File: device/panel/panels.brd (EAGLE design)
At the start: 133 x 77 mm, 0 parts

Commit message: More panel work.
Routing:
- added copper zone on layer 16, net S$1
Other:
- board size 133 x 77 mm -> 132.9 x 80 mm

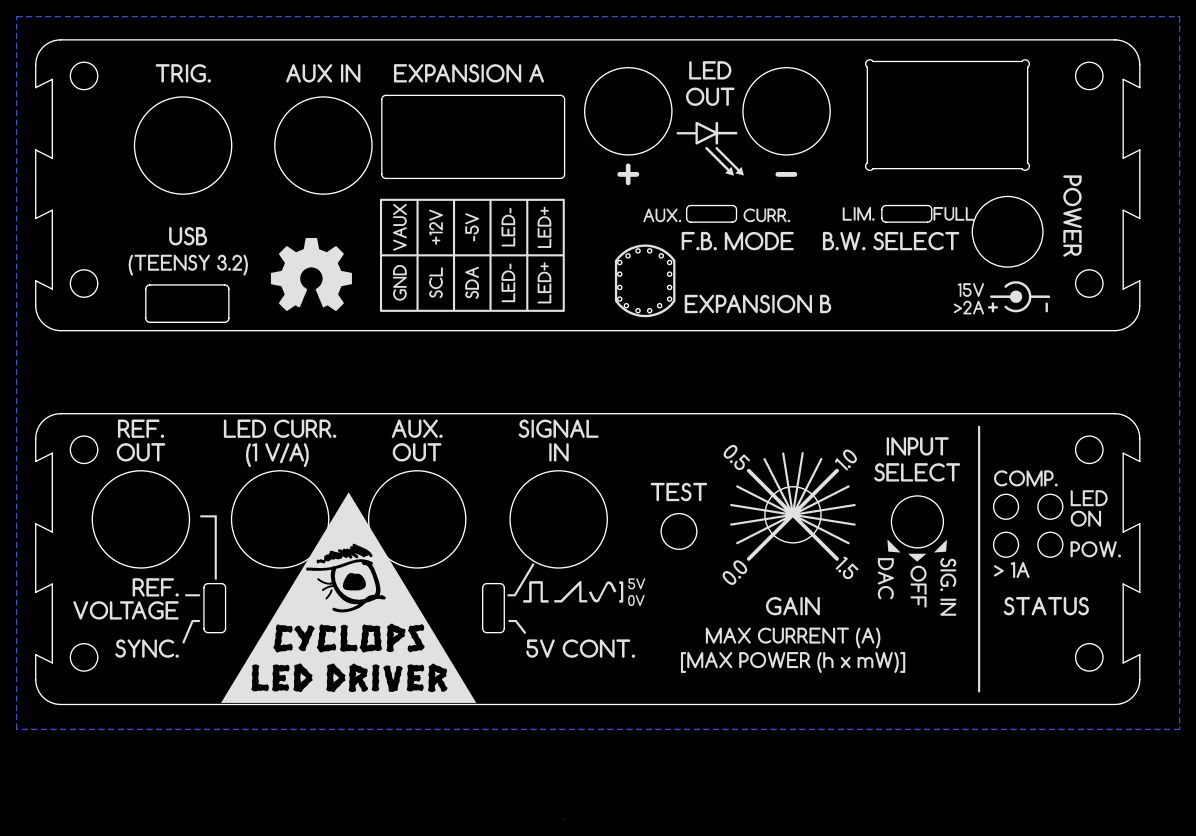
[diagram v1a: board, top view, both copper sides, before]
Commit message: Panels and final protoboard sent to production.
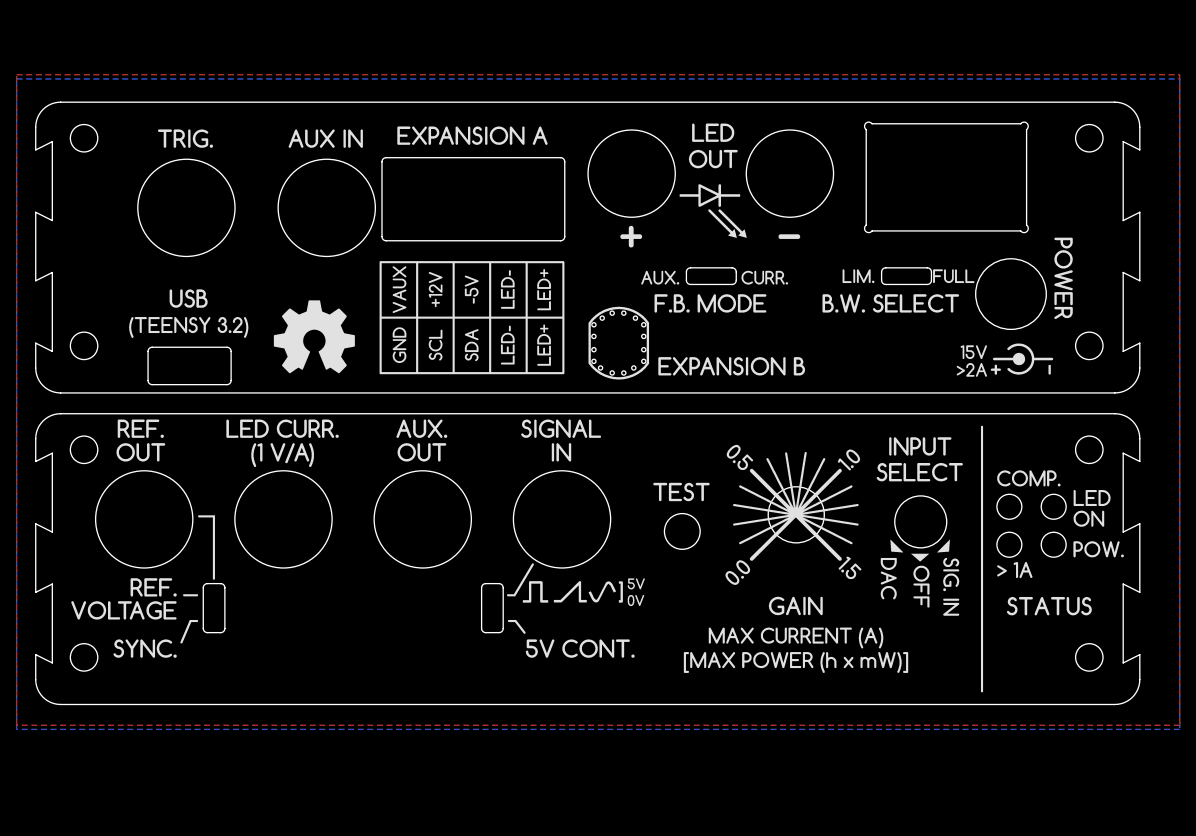
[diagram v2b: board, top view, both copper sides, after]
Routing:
- added copper zone on layer 1, net S$1
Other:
- board size 132.9 x 80 mm -> 132.9 x 72.5 mm

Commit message: Panel fixes after testing.
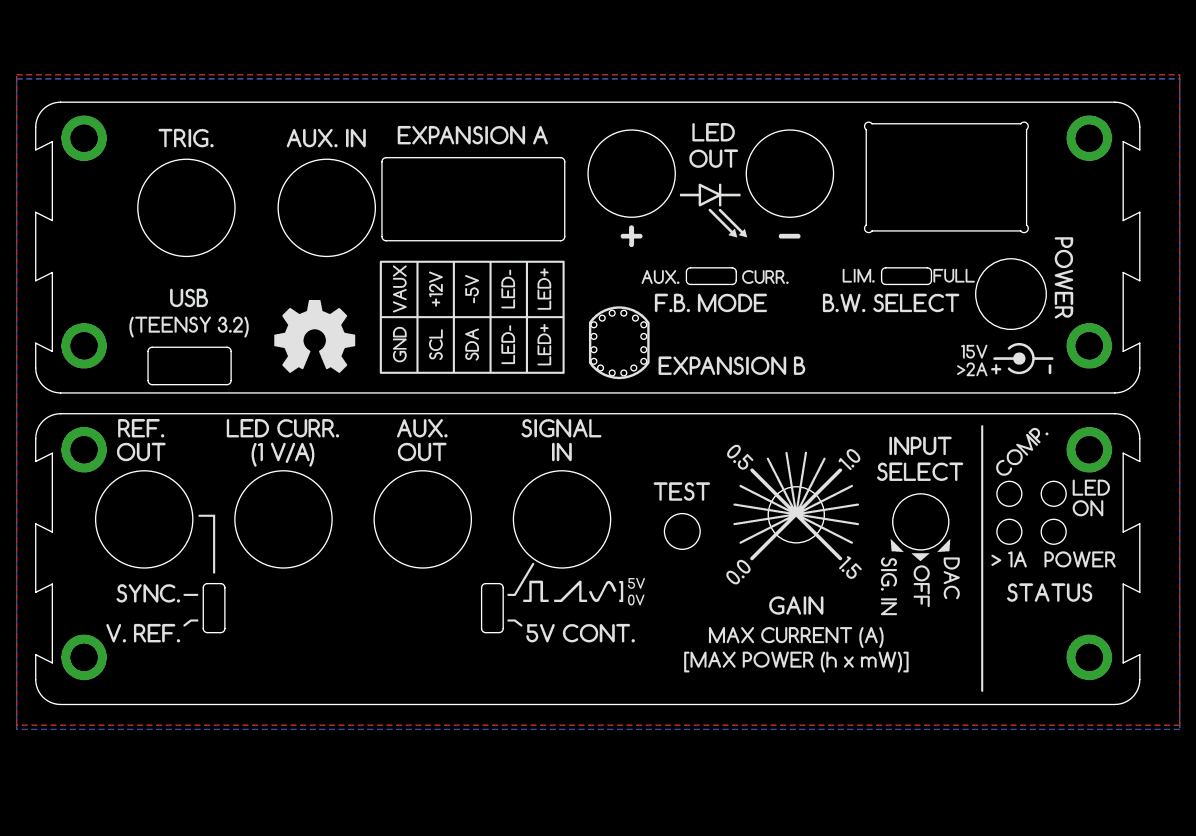
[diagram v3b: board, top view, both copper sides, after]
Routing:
- added copper zone on layer 1, net GND
- added copper zone on layer 16, net GND
- removed copper zone on layer 1, net S$1
- removed copper zone on layer 16, net S$1

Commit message: Ready for 3.6 production
- These designs are up to date for 3.6 production
- I need to create an assembly manual before moving forward
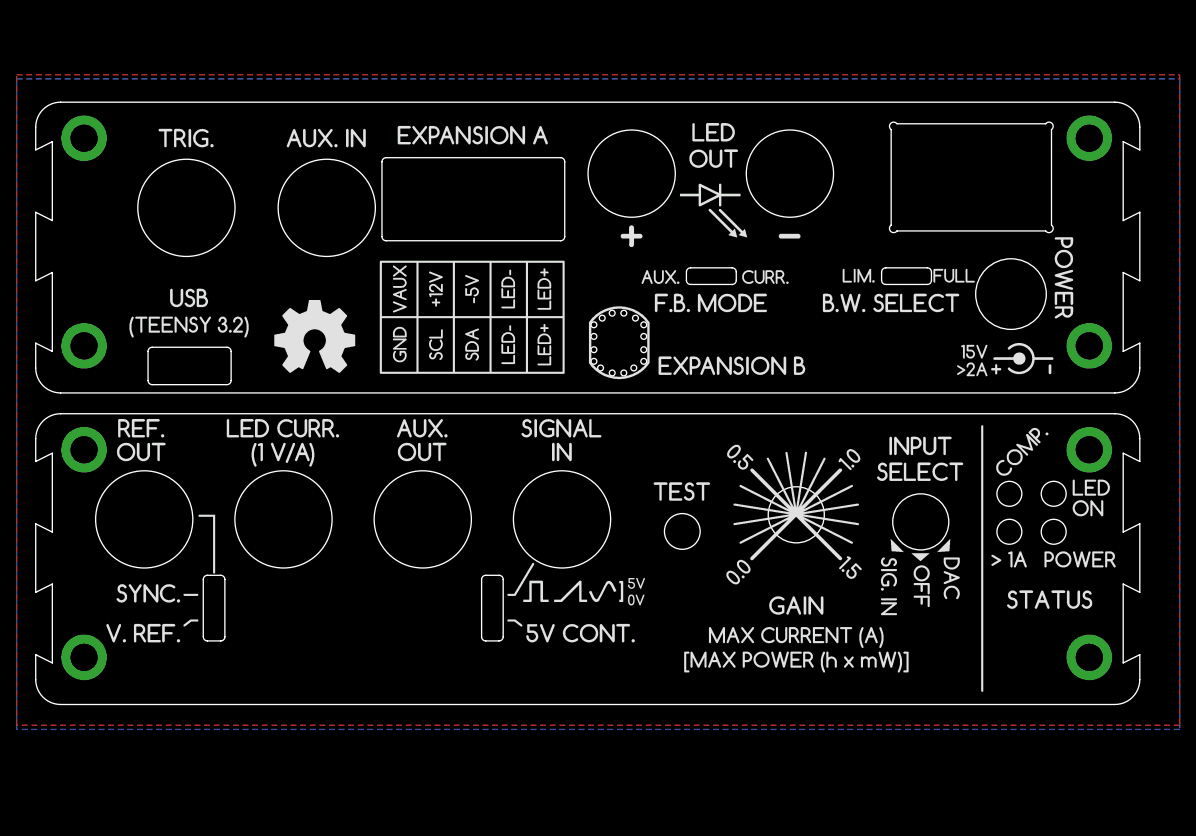
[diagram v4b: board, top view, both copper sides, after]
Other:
- outline, holes or cut-outs redrawn
